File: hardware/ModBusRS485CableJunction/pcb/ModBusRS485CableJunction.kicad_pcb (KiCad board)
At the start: 2 copper layers, 6 parts, among them J1 215877-1, J2 Modbus Stub

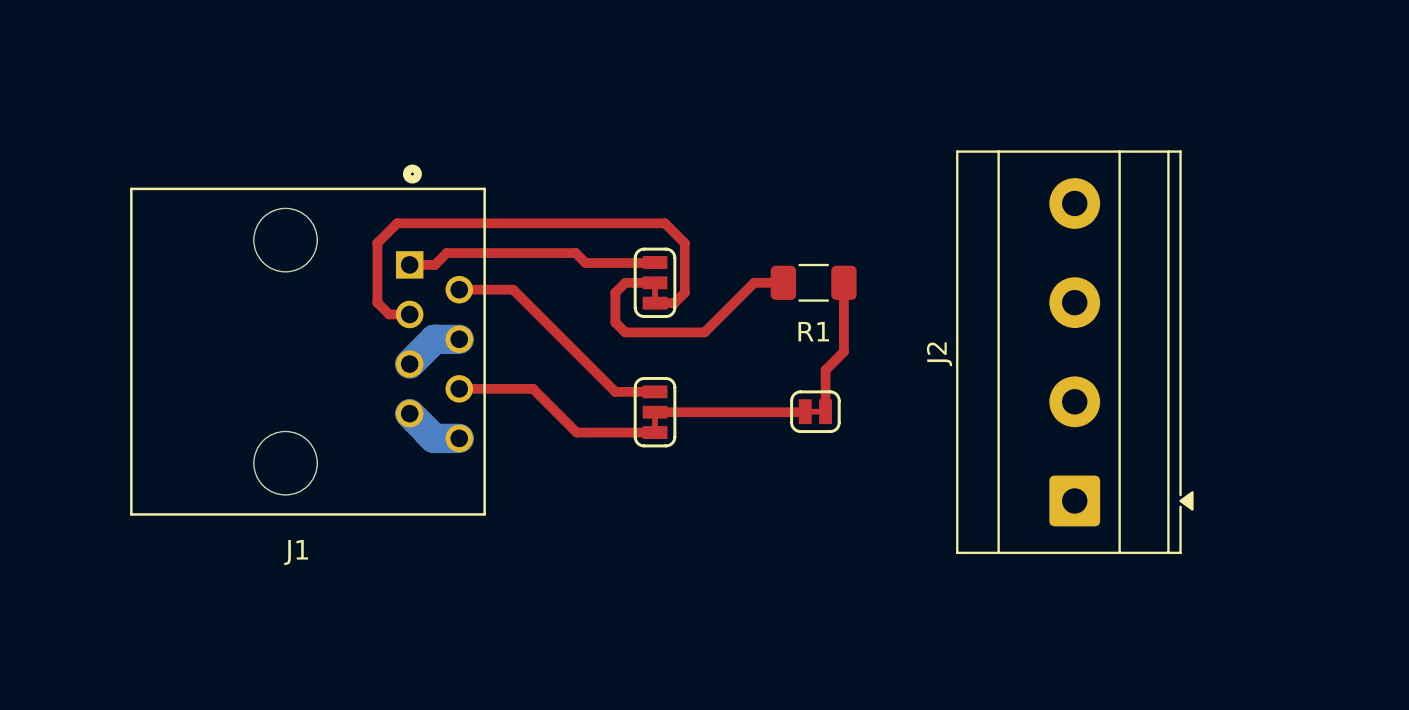
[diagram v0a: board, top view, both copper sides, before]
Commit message: Updated PCB for modbus cabling
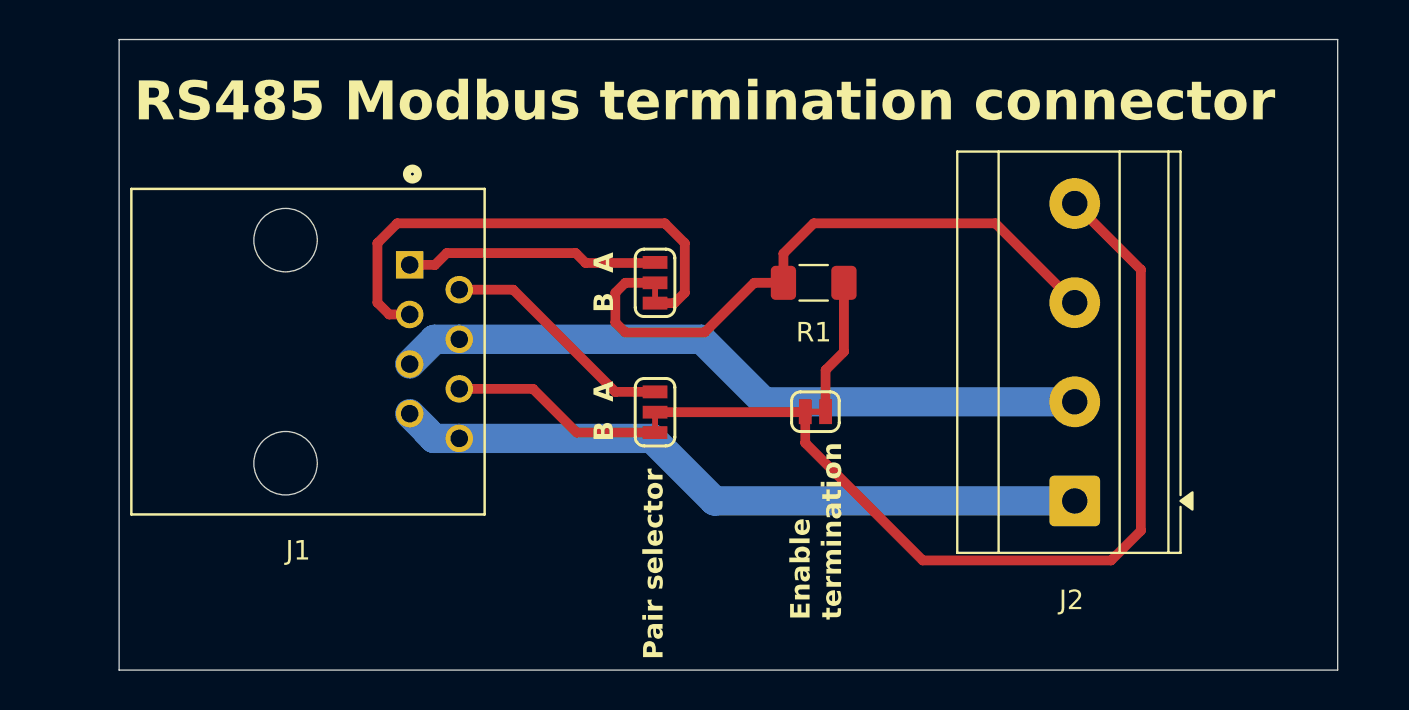
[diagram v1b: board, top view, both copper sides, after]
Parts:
- added G***: LOGO_LogoRFSee_37x8mm, my-KiCad-library:LOGO_LogoRFSee_37x8mm, F.Cu at (152.4, 120.9)
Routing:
- net /B: track 7.71 -> 47.8 mm
- net /GND: track 3.08 -> 35.9 mm
- net /24V: track 3.07 -> 35.9 mm
- net /A: track 13.6 -> 32.4 mm
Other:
- board outline added: 62.4 x 32.3 mm
- board text added: "A"
- board text added: "B"
- board text added: "Enable termination"
- board text added: "Pair selector"
- board text added: "RS485 Modbus termination connector"

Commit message: added text silkscreen
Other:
- board text added: "24V"
- board text added: "GND"
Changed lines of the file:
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@@
+		)
+	)
+	(gr_text "B"
+		(at 180.848 101.6 90)
+		(layer "F.SilkS")
+		(effects
+			(font
+				(size 1.5 1.5)
+				(thickness 0.3)
+				(bold yes)
+			)
+			(justify bottom)
+		)
+	)
+	(gr_text "A"
+		(at 180.848 106.68 90)
+		(layer "F.SilkS")
+		(effects
+			(font
+				(size 1.5 1.5)
+				(thickness 0.3)
+				(bold yes)
+			)
+			(justify bottom)
+		)
+	)
+	(gr_text "24V"
+		(at 180.848 111.76 90)
+		(layer "F.SilkS")
+		(effects
+			(font
+				(size 1.5 1.5)
+				(thickness 0.3)
+				(bold yes)
+			)
+			(justify bottom)
+		)
+	)
+	(gr_text "GND"
+		(at 180.848 116.84 90)
+		(layer "F.SilkS")
+		(effects
+			(font
+				(size 1.5 1.5)
+				(thickness 0.3)
+				(bold yes)
+			)
+			(justify bottom)
 		)
 	)
